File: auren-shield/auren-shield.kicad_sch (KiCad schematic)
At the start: 45 parts, among them J1 Tympan_SJ-3523-SMT-TR, J2 Tympan_SJ-3524-SMT-TR-PI, J3 HDMI A, J5 Conn_01x01, J6 Conn_01x01, P1 CONN_01X06, P2 CONN_01X06, P3 CONN_01X06, P4 CONN_01X06, P5 CONN_01X06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

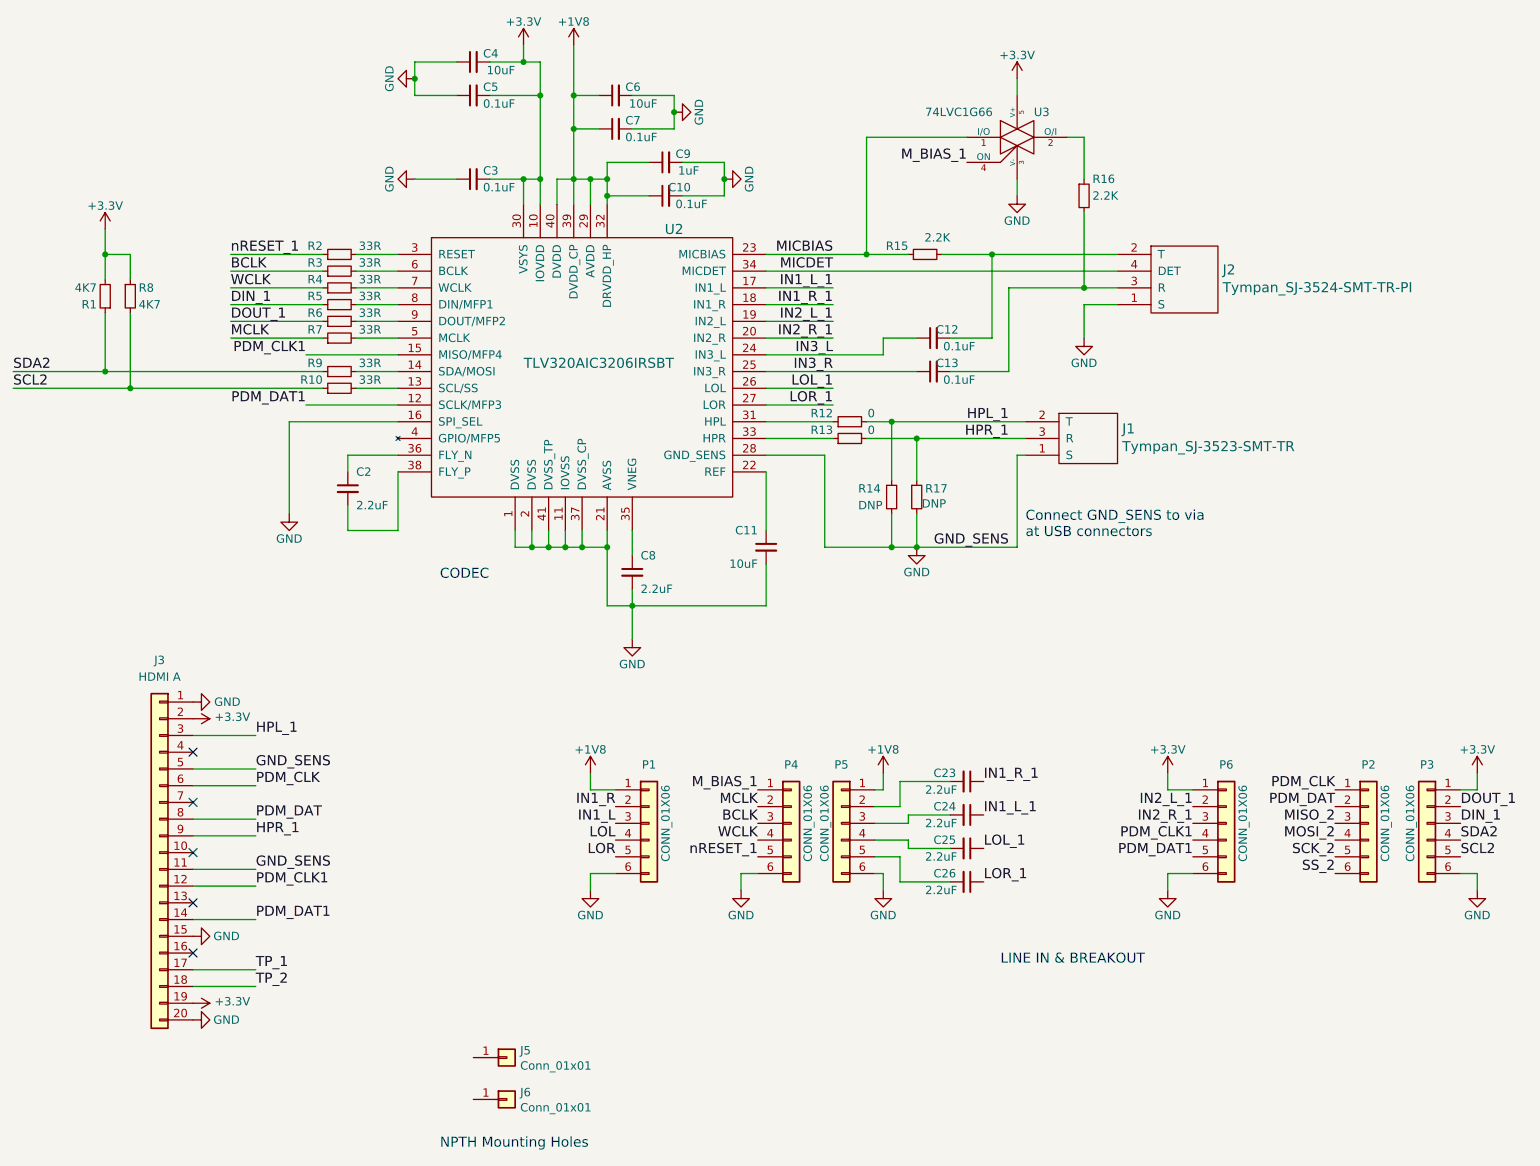
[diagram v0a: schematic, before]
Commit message: HDMI A connector routing
also moved the Rs and Cs above the AIC closer to it. There is some room to move the HDMI left and down to shorten the board, but also crowd the layout. tradeoffs.
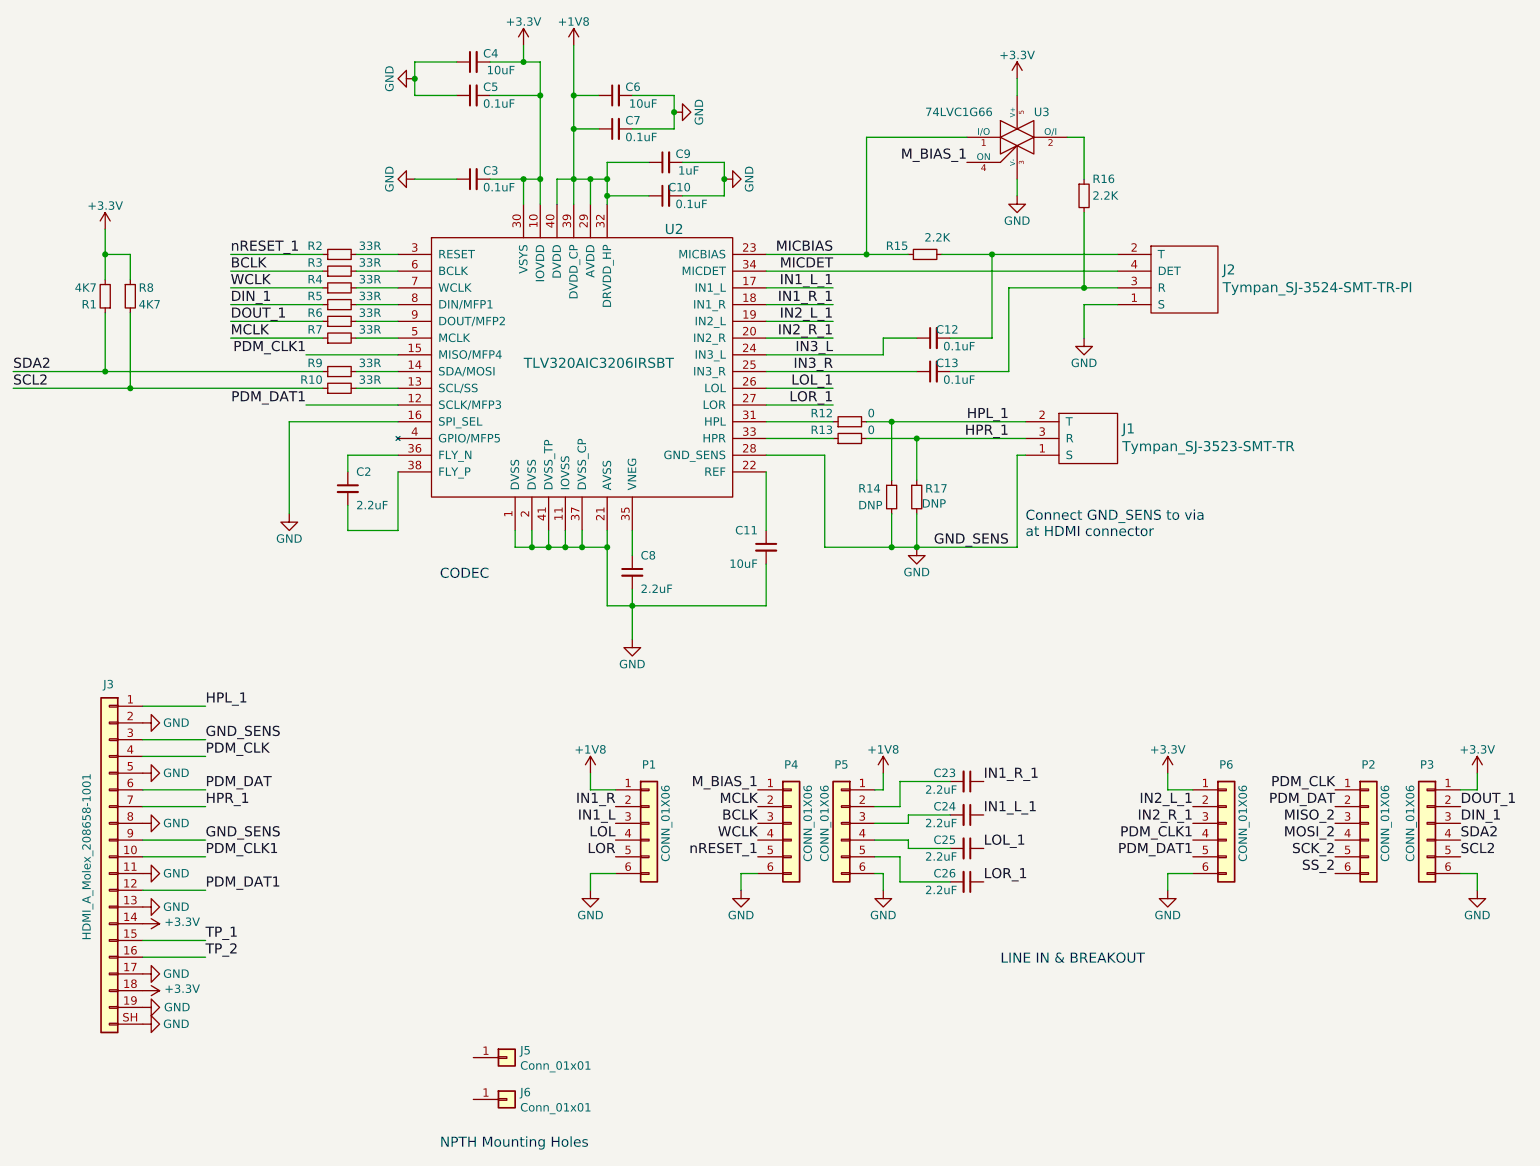
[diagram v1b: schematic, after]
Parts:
- J3: value HDMI A -> HDMI_A_Molex_208658-1001; footprint (none) -> Connector_Video:HDMI_A_Molex_208658-1001_Horizontal
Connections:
- net +3.3V: now also J3.14 (Pin_14), J3.18 (Pin_18); no longer J3.19 (Pin_19), J3.2 (Pin_2)
- net GND: now also J3.13 (Pin_13), J3.17 (Pin_17), J3.19 (Pin_19), J3.2 (Pin_2), J3.3 (Pin_3), J3.8 (Pin_8), J3.9 (Pin_9), J3.SH (Pin_20); no longer J3.1 (Pin_1), J3.15 (Pin_15), J3.20 (Pin_20)
- net HPL_1: now also J3.1 (Pin_1); no longer J3.3 (Pin_3)
- net HPR_1: now also J3.7 (Pin_7); no longer J3.9 (Pin_9)
- net PDM_CLK: now also J3.4 (Pin_4); no longer J3.6 (Pin_6)
- net PDM_CLK1: now also J3.10 (Pin_10); no longer J3.12 (Pin_12)
- net PDM_DAT: now also J3.6 (Pin_6); no longer J3.8 (Pin_8)
- net PDM_DAT1: now also J3.12 (Pin_12); no longer J3.14 (Pin_14)
- net TP_1: now also J3.15 (Pin_15); no longer J3.17 (Pin_17)
- net TP_2: now also J3.16 (Pin_16); no longer J3.18 (Pin_18)
- no-connect marks 5 -> 0
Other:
- note added: "Connect GND_SENS to via at HDMI connector"
- note removed: "Connect GND_SENS to via at USB connectors"
- title: Tympan EarPiece Shield -> Tympan Auren Shield
- moved on the sheet: J3

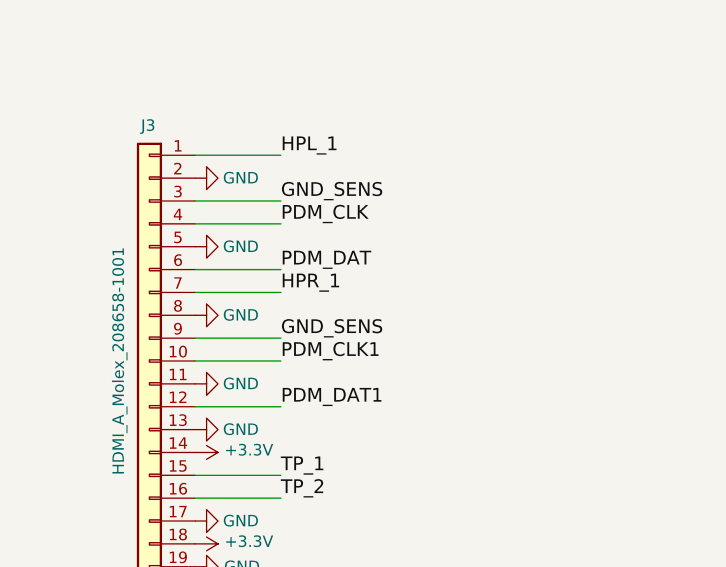
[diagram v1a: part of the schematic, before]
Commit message: added Rs per #5
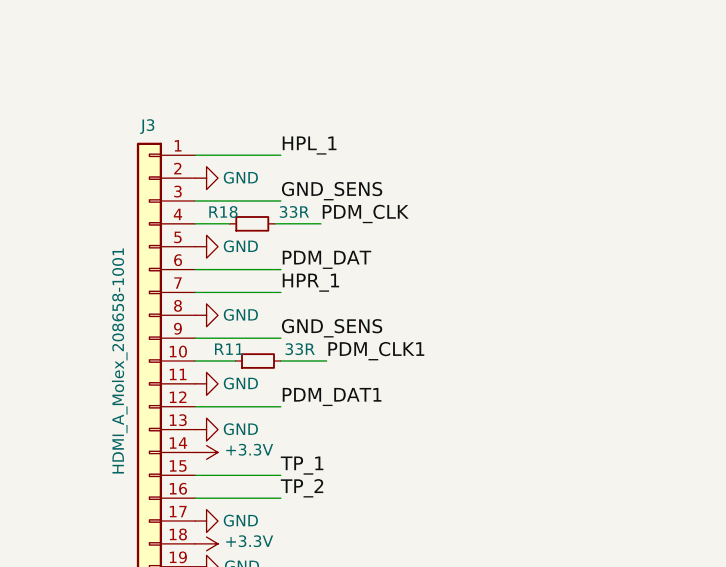
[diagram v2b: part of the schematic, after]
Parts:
- added R11, R18: 33R, Resistor_SMD:R_0402_1005Metric, symbol Device:R_Small
- C10, C11, C12, C13, C2, C24, C25, C26, C3, C4, C5, C6, C7, C8, C9: footprint Capacitors_SMD:C_0402 -> Capacitor_SMD:C_0402_1005Metric
- R1, R10, R2, R3, R4, R5, R6, R7, R8, R9: footprint Resistors_SMD:R_0402 -> Resistor_SMD:R_0402_1005Metric
- R12, R13, R14, R15, R16, R17: footprint Capacitors_SMD:C_0603 -> Resistor_SMD:R_0603_1608Metric
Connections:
- net PDM_CLK: now also R18.2; no longer J3.4 (Pin_4)
- net PDM_CLK1: now also R11.2; no longer J3.10 (Pin_10)
- new net: J3.10 (Pin_10), R11.1
- new net: J3.4 (Pin_4), R18.1
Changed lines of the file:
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@@
 	(wire
 		(pts
+			(xy 69.85 69.85) (xy 83.82 69.85)
+		)
+		(stroke
+			(width 0)
+			(type default)
+		)
+	)
+	(wire
+		(pts
 			(xy 133.35 45.72) (xy 127 45.72)
 		)
@@
 	(wire
 		(pts
-			(xy 45.085 146.05) (xy 54.61 146.05)
-		)
-		(stroke
-			(width 0)
-			(type default)
-		)
-	)
-	(wire
-		(pts
 			(xy 72.39 59.69) (xy 58.42 59.69)
 		)
@@
 	(wire
 		(pts
-			(xy 54.61 130.81) (xy 45.085 130.81)
-		)
-		(stroke
-			(width 0)
-			(type default)
-		)
-	)
-	(wire
-		(pts
 			(xy 54.61 143.51) (xy 45.085 143.51)
 		)
@@
 	(wire
 		(pts
-			(xy 69.85 69.85) (xy 83.82 69.85)
+			(xy 45.085 146.05) (xy 49.53 146.05)
 		)
 		(stroke
@@
 	(wire
 		(pts
+			(xy 45.085 130.81) (xy 48.895 130.81)
+		)
+		(stroke
+			(width 0)
+			(type default)
+		)
+	)
+	(wire
+		(pts
 			(xy 125.73 35.56) (xy 119.38 35.56)
 		)
@@
 	(wire
 		(pts
+			(xy 53.975 130.81) (xy 59.055 130.81)
+		)
+		(stroke
+			(width 0)
+			(type default)
+		)
+	)
+	(wire
+		(pts
 			(xy 105.41 43.18) (xy 105.41 46.99)
 		)
@@
 	(wire
 		(pts
+			(xy 54.61 146.05) (xy 59.69 146.05)
+		)
+		(stroke
+			(width 0)
+			(type default)
+		)
+	)
+	(wire
+		(pts
 			(xy 43.18 63.5) (xy 43.18 74.93)
 		)
@@
 	)
 	(label "PDM_CLK1"
-		(at 54.61 146.05 0)
+		(at 59.69 146.05 0)
 		(effects
 			(font
@@
 	)
 	(label "PDM_CLK"
-		(at 54.61 130.81 0)
+		(at 59.055 130.81 0)
 		(effects
 			(font
@@
 			)
 		)
-		(property "Footprint" "Capacitors_SMD:C_0603"
+		(property "Footprint" "Resistor_SMD:R_0603_1608Metric"
 			(at 152.4 80.01 0)
 			(effects
@@
 			)
 		)
-		(property "Footprint" "Capacitors_SMD:C_0603"
+		(property "Footprint" "Resistor_SMD:R_0603_1608Metric"
 			(at 152.4 82.55 0)
 			(effects
@@
 			)
 		)
-		(property "Footprint" "Capacitors_SMD:C_0603"
+		(property "Footprint" "Resistor_SMD:R_0603_1608Metric"
 			(at 158.75 91.44 0)
 			(effects
@@
 			)
 		)
-		(property "Footprint" "Capacitors_SMD:C_0603"
+		(property "Footprint" "Resistor_SMD:R_0603_1608Metric"
 			(at 162.56 91.44 0)
 			(effects
@@
 			)
 		)
-		(property "Footprint" "Resistors_SMD:R_0402"
+		(property "Footprint" "Resistor_SMD:R_0402_1005Metric"
 			(at 74.93 54.61 0)
 			(effects
@@
 			)
 		)
-		(property "Footprint" "Resistors_SMD:R_0402"
+		(property "Footprint" "Resistor_SMD:R_0402_1005Metric"
 			(at 74.93 57.15 0)
 			(effects
@@
 			)
 		)
-		(property "Footprint" "Resistors_SMD:R_0402"
+		(property "Footprint" "Resistor_SMD:R_0402_1005Metric"
 			(at 74.93 59.69 0)
 			(effects
@@
 			)
 		)
-		(property "Footprint" "Resistors_SMD:R_0402"
+		(property "Footprint" "Resistor_SMD:R_0402_1005Metric"
 			(at 74.93 62.23 0)
 			(effects
@@
 			)
 		)
-		(property "Footprint" "Resistors_SMD:R_0402"
+		(property "Footprint" "Resistor_SMD:R_0402_1005Metric"
 			(at 74.93 64.77 0)
 			(effects
@@
 			)
 		)
-		(property "Footprint" "Resistors_SMD:R_0402"
+		(property "Footprint" "Resistor_SMD:R_0402_1005Metric"
 			(at 74.93 67.31 0)
 			(effects
@@
 			)
 		)
-		(property "Footprint" "Resistors_SMD:R_0402"
+		(property "Footprint" "Resistor_SMD:R_0402_1005Metric"
 			(at 74.93 72.39 0)
 			(effects
@@
 			)
 		)
-		(property "Footprint" "Resistors_SMD:R_0402"
+		(property "Footprint" "Resistor_SMD:R_0402_1005Metric"
 			(at 74.93 74.93 0)
 			(effects
@@
 			)
 		)
-		(property "Footprint" "Capacitors_SMD:C_0402"
+		(property "Footprint" "Capacitor_SMD:C_0402_1005Metric"
 			(at 139.7 99.06 0)
 			(effects
@@
 			)
 		)
-		(property "Footprint" "Capacitors_SMD:C_0402"
+		(property "Footprint" "Capacitor_SMD:C_0402_1005Metric"
 			(at 119.38 102.87 0)
 			(effects
@@
 			)
 		)
-		(property "Footprint" "Capacitors_SMD:C_0402"
+		(property "Footprint" "Capacitor_SMD:C_0402_1005Metric"
 			(at 76.2 90.17 0)
 			(effects
@@
 			)
 		)
-		(property "Footprint" "Capacitors_SMD:C_0402"
+		(property "Footprint" "Capacitor_SMD:C_0402_1005Metric"
 			(at 95.25 25.4 0)
 			(effects
@@
 			)
 		)
-		(property "Footprint" "Capacitors_SMD:C_0402"
+		(property "Footprint" "Capacitor_SMD:C_0402_1005Metric"
 			(at 95.25 30.48 0)
 			(effects
@@
 			)
 		)
-		(property "Footprint" "Capacitors_SMD:C_0402"
+		(property "Footprint" "Capacitor_SMD:C_0402_1005Metric"
 			(at 116.84 35.56 0)
 			(effects
@@
 			)
 		)
-		(property "Footprint" "Capacitors_SMD:C_0402"
+		(property "Footprint" "Capacitor_SMD:C_0402_1005Metric"
 			(at 116.84 30.48 0)
 			(effects
@@
 			)
 		)
-		(property "Footprint" "Capacitors_SMD:C_0402"
+		(property "Footprint" "Capacitor_SMD:C_0402_1005Metric"
 			(at 124.46 40.64 0)
 			(effects
@@
 			)
 		)
-		(property "Footprint" "Capacitors_SMD:C_0402"
+		(property "Footprint" "Capacitor_SMD:C_0402_1005Metric"
 			(at 124.46 45.72 0)
 			(effects
@@
 			)
 		)
-		(property "Footprint" "Capacitors_SMD:C_0402"
+		(property "Footprint" "Capacitor_SMD:C_0402_1005Metric"
 			(at 95.25 43.18 0)
 			(effects
@@
 			)
 		)
-		(property "Footprint" "Capacitors_SMD:C_0402"
+		(property "Footprint" "Capacitor_SMD:C_0402_1005Metric"
 			(at 170.18 139.7 0)
 			(effects
@@
 			)
 		)
-		(property "Footprint" "Capacitors_SMD:C_0402"
+		(property "Footprint" "Capacitor_SMD:C_0402_1005Metric"
 			(at 170.18 144.78 0)
 			(effects
@@
 			)
 		)
-		(property "Footprint" "Capacitors_SMD:C_0402"
+		(property "Footprint" "Capacitor_SMD:C_0402_1005Metric"
 			(at 170.18 149.86 0)
 			(effects
@@
 			)
 		)
-		(property "Footprint" "Resistors_SMD:R_0402"
+		(property "Footprint" "Resistor_SMD:R_0402_1005Metric"
 			(at 43.18 60.96 0)
 			(effects
@@
 			)
 		)
-		(property "Footprint" "Resistors_SMD:R_0402"
+		(property "Footprint" "Resistor_SMD:R_0402_1005Metric"
 			(at 39.37 60.96 0)
 			(effects
@@
 			)
 		)
-		(property "Footprint" "Capacitors_SMD:C_0603"
+		(property "Footprint" "Resistor_SMD:R_0603_1608Metric"
 			(at 163.83 54.61 0)
 			(effects
@@
 			)
 		)
-		(property "Footprint" "Capacitors_SMD:C_0603"
+		(property "Footprint" "Resistor_SMD:R_0603_1608Metric"
 			(at 187.96 45.72 0)
 			(effects
@@
 			)
 		)
-		(property "Footprint" "Capacitors_SMD:C_0402"
+		(property "Footprint" "Capacitor_SMD:C_0402_1005Metric"
 			(at 165.1 72.39 0)
 			(effects
@@
 			)
 		)
-		(property "Footprint" "Capacitors_SMD:C_0402"
+		(property "Footprint" "Capacitor_SMD:C_0402_1005Metric"
 			(at 165.1 67.31 0)
 			(effects
@@
 	)
 	(symbol
+		(lib_id "Device:R_Small")
+		(at 51.435 130.81 90)
+		(unit 1)
+		(exclude_from_sim no)
+		(in_bom yes)
+		(on_board yes)
+		(dnp no)
+		(property "Reference" "R18"
+			(at 49.911 129.54 90)
+			(effects
+				(font
+					(size 1.27 1.27)
+				)
+				(justify left)
+			)
+		)
+		(property "Value" "33R"
+			(at 57.785 129.54 90)
+			(effects
+				(font
+					(size 1.27 1.27)
+				)
+				(justify left)
+			)
+		)
+		(property "Footprint" "Resistor_SMD:R_0402_1005Metric"
+			(at 51.435 130.81 0)
+			(effects
+				(font
+					(size 1.27 1.27)
+				)
+				(hide yes)
+			)
+		)
+		(property "Datasheet" ""
+			(at 51.435 130.81 0)
+			(effects
+				(font
+					(size 1.27 1.27)
+				)
+			)
+		)
+		(property "Description" ""
+			(at 51.435 130.81 0)
+			(effects
+				(font
+					(size 1.27 1.27)
+				)
+			)
+		)
+		(pin "1"
+		)
+		(pin "2"
+		)
+		(instances
+			(project "auren-shield"
+				(path "/2aef2ae4-0dbd-424b-8fd8-1bf240a2e15b"
+					(reference "R18")
+					(unit 1)
+				)
+			)
+		)
+	)
+	(symbol
 		(lib_id "power:GND")
 		(at 45.085 171.45 90)
@@
 					(unit 1)
 				)
+			)
+		)
+	)
+	(symbol
+		(lib_id "Device:R_Small")
+		(at 52.07 146.05 90)
+		(unit 1)
+		(exclude_from_sim no)
+		(in_bom yes)
+		(on_board yes)
+		(dnp no)
+		(property "Reference" "R11"
+			(at 50.546 144.78 90)
+			(effects
+				(font
+					(size 1.27 1.27)
+				)
+				(justify left)
+			)
+		)
+		(property "Value" "33R"
+			(at 58.42 144.78 90)
+			(effects
+				(font
+					(size 1.27 1.27)
+				)
+				(justify left)
+			)
+		)
+		(property "Footprint" "Resistor_SMD:R_0402_1005Metric"
+			(at 52.07 146.05 0)
+			(effects
+				(font
+					(size 1.27 1.27)
+				)
+				(hide yes)
+			)
+		)
+		(property "Datasheet" ""
+			(at 52.07 146.05 0)
+			(effects
+				(font
+					(size 1.27 1.27)
+				)
+			)
+		)
+		(property "Description" ""
+			(at 52.07 146.05 0)
+			(effects
+				(font
+					(size 1.27 1.27)
+				)
+			)
+		)
+		(pin "1"
+		)
+		(pin "2"
+		)
+		(instances
+			(project "auren-shield"
+				(path "/2aef2ae4-0dbd-424b-8fd8-1bf240a2e15b"
+					(reference "R11")
+					(unit 1)
+				)
